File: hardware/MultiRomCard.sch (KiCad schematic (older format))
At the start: 18 parts, among them P1 VC4000_Cartridge_Bus, P2 MicroSD_Breakout, P3 Test Header, U1 Arduino_Nano, U2 74HC595, U3 74HC595, U4 74HC595, U5 6264, U6 74HC245, U7 74HC245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

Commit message: [SCH/PCB] Rotate MicroSD breakout header.
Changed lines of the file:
@@
 Sheet 1 1
 Title "Interton VC4000 MultiRom Cartridge"
-Date "Wednesday, July 22, 2015"
+Date "Tuesday, July 28, 2015"
 Rev "0.1"
 Comp "Mario Keller and Johannes Maibaum"
@@
 	1600 2350 1600 1650
 Wire Wire Line
-	1500 2250 2600 2250
-Wire Wire Line
-	2600 2250 2600 3300
+	2600 1950 2600 3300
 Wire Wire Line
 	2600 3300 2200 3300
 Wire Wire Line
-	1500 1950 2300 1950
-Wire Wire Line
-	2300 1950 2300 3000
-Wire Wire Line
-	2300 3000 2200 3000
-Wire Wire Line
-	1500 2050 2400 2050
-Wire Wire Line
-	2400 2050 2400 3100
-Wire Wire Line
-	2400 3100 2200 3100
+	2200 3000 2300 3000
+Wire Wire Line
+	1500 2050 2300 2050
+Wire Wire Line
+	2300 2050 2300 3000
 Wire Wire Line
 	1500 2150 2500 2150
@@
 	1    1600 1650
 	1    0    0    -1
-$EndComp
-$Comp
-L MicroSD_Breakout P2
-U 1 1 55880347
-P 1300 2200
-F 0 "P2" H 1400 2550 60  0000 C CNN
-F 1 "MicroSD_Breakout" V 1600 2200 60  0000 C CNN
-F 2 "Pin_Headers:Pin_Header_Straight_1x06" H 1300 2200 60  0001 C CNN
-F 3 "" H 1300 2200 60  0000 C CNN
-	1    1300 2200
-	-1   0    0    -1
 $EndComp
 NoConn ~ 900  3800
@@
 Wire Wire Line
 	9750 3750 9750 3900
+$Comp
+L MicroSD_Breakout P2
+U 1 1 55B39402
+P 1300 2200
+F 0 "P2" H 1400 2550 60  0000 C CNN
+F 1 "MicroSD_Breakout" V 1600 2200 60  0000 C CNN
+F 2 "Pin_Headers:Pin_Header_Straight_1x06" H 1300 2200 60  0001 C CNN
+F 3 "" H 1300 2200 60  0000 C CNN
+	1    1300 2200
+	-1   0    0    -1
+$EndComp
+Wire Wire Line
+	2600 1950 1500 1950
+Wire Wire Line
+	1500 2250 2400 2250
+Wire Wire Line
+	2400 2250 2400 3100
+Wire Wire Line
+	2400 3100 2200 3100
 $EndSCHEMATC

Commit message: [HW/FW] Incorporate latest changes into hardware and firmware.
- From now on, we should call the hardware rev. 0.2.
- All games should now work (ROM and ROM+RAM)
- Up to 6K (5.5K) ROM is currently allowed (7.5K should be
  possible, too, with one line change in the FW.)
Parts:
- removed P3: Test Header, Pin_Headers:Pin_Header_Straight_1x30, symbol CONN_01X30
- added C8, C9: .1uF, Capacitors_ThroughHole:C_Disc_D6_P5, symbol C
- added R1: 10k, Resistors_ThroughHole:Resistor_Horizontal_RM10mm, symbol R
- added U10: 74HC32, Housings_DIP:DIP-14_W7.62mm_LongPads, symbol 74LS32
- added U9: 74HC00, Housings_DIP:DIP-14_W7.62mm_LongPads, symbol 74HC00
- U2, U3, U4: footprint Housings_DIP:DIP-16__300_ELL -> Housings_DIP:DIP-16_W7.62mm_LongPads
- U5: footprint Housings_DIP:DIP-28__600_ELL -> Housings_DIP:DIP-28_W15.24mm_LongPads
- U6, U7, U8: footprint Housings_DIP:DIP-20__300_ELL -> Housings_DIP:DIP-20_W7.62mm_LongPads
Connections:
- net labels added: CE1, CEDBUS, RW, WCONTROL, WRP
- net labels removed: CE1SRAM, CE2, CE2SRAM, P26, P27, P28, PVISEL
- wire segments 236 -> 204
- no-connect marks 20 -> 24
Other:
- moved on the sheet: C1, C2, C3, C4, C5, C6, C7, U6, U7, U8

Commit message: [HW] A little cleanup on the schematic, new PDF printouts.
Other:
- moved on the sheet: R1, U10A, U9A
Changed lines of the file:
@@
 Sheet 1 1
 Title "Interton VC4000 MultiRom Cartridge"
-Date "Monday, August 3, 2015"
+Date "Tuesday, August 4, 2015"
 Rev "0.2"
 Comp "Mario Keller and Johannes Maibaum"
@@
 	1    0    0    -1
 $EndComp
-Text GLabel 6700 3700 2    48   Input ~ 0
+Text GLabel 6700 3500 2    48   Input ~ 0
 WESRAM
 Text GLabel 2200 3300 2    48   Output ~ 0
@@
 Text GLabel 9500 3350 1    48   Input ~ 0
 OEVCBUS
-Text GLabel 5500 4700 0    48   Input ~ 0
+Text GLabel 5500 5150 0    48   Input ~ 0
 OEVCBUS
 Text GLabel 9550 1400 2    48   Input ~ 0
@@
 L R R1
 U 1 1 55BBBA81
-P 7150 3750
-F 0 "R1" V 7230 3750 50  0000 C CNN
-F 1 "10k" V 7150 3750 50  0000 C CNN
-F 2 "Resistors_ThroughHole:Resistor_Horizontal_RM10mm" V 7080 3750 30  0001 C CNN
-F 3 "" H 7150 3750 30  0000 C CNN
-	1    7150 3750
+P 7150 3900
+F 0 "R1" V 7230 3900 50  0000 C CNN
+F 1 "10k" V 7150 3900 50  0000 C CNN
+F 2 "Resistors_ThroughHole:Resistor_Horizontal_RM10mm" V 7080 3900 30  0001 C CNN
+F 3 "" H 7150 3900 30  0000 C CNN
+	1    7150 3900
 	1    0    0    -1
 $EndComp
@@
 L GND #PWR012
 U 1 1 55BBBD64
-P 7150 3900
-F 0 "#PWR012" H 7150 3900 30  0001 C CNN
-F 1 "GND" H 7150 3830 30  0001 C CNN
-F 2 "" H 7150 3900 60  0000 C CNN
-F 3 "" H 7150 3900 60  0000 C CNN
-	1    7150 3900
+P 7150 4050
+F 0 "#PWR012" H 7150 4050 30  0001 C CNN
+F 1 "GND" H 7150 3980 30  0001 C CNN
+F 2 "" H 7150 4050 60  0000 C CNN
+F 3 "" H 7150 4050 60  0000 C CNN
+	1    7150 4050
 	1    0    0    -1
 $EndComp
@@
 L 74HC00 U9
 U 1 1 55BBD9BC
-P 6100 4100
-F 0 "U9" H 6100 4150 60  0000 C CNN
-F 1 "74HC00" H 6100 4050 60  0000 C CNN
-F 2 "Housings_DIP:DIP-14_W7.62mm_LongPads" H 6100 4100 60  0001 C CNN
-F 3 "" H 6100 4100 60  0000 C CNN
-	1    6100 4100
+P 6100 4550
+F 0 "U9" H 6100 4600 60  0000 C CNN
+F 1 "74HC00" H 6100 4500 60  0000 C CNN
+F 2 "Housings_DIP:DIP-14_W7.62mm_LongPads" H 6100 4550 60  0001 C CNN
+F 3 "" H 6100 4550 60  0000 C CNN
+	1    6100 4550
 	-1   0    0    -1
 $EndComp
@@
 L 74LS32 U10
 U 1 1 55BBDA1A
-P 6100 4600
-F 0 "U10" H 6100 4650 60  0000 C CNN
-F 1 "74HC32" H 6100 4550 60  0000 C CNN
-F 2 "Housings_DIP:DIP-14_W7.62mm_LongPads" H 6100 4600 60  0001 C CNN
-F 3 "" H 6100 4600 60  0000 C CNN
-	1    6100 4600
+P 6100 5050
+F 0 "U10" H 6100 5100 60  0000 C CNN
+F 1 "74HC32" H 6100 5000 60  0000 C CNN
+F 2 "Housings_DIP:DIP-14_W7.62mm_LongPads" H 6100 5050 60  0001 C CNN
+F 3 "" H 6100 5050 60  0000 C CNN
+	1    6100 5050
 	1    0    0    -1
 $EndComp
 Text GLabel 9600 4850 2    48   Input ~ 0
 CEDBUS
-Text GLabel 6700 4600 2    48   Output ~ 0
+Text GLabel 6700 5050 2    48   Output ~ 0
 CEDBUS
 $Comp
@@
 U 2 1 55BC3174
 P 9150 850
-F 0 "U9" H 9150 800 60  0000 C CNN
-F 1 "74HC00" H 9150 900 60  0000 C CNN
+F 0 "U9" H 9150 900 60  0000 C CNN
+F 1 "74HC00" H 9150 800 60  0000 C CNN
 F 2 "Housings_DIP:DIP-14_W7.62mm_LongPads" H 9150 850 60  0001 C CNN
 F 3 "" H 9150 850 60  0000 C CNN
 	2    9150 850
-	-1   0    0    1
-$EndComp
+	-1   0    0    -1
+$EndComp
+Text Label 9750 950  0    60   ~ 0
+WRP
 Text Label 9750 750  0    60   ~ 0
-WRP
-Text Label 9750 950  0    60   ~ 0
 RW
 Entry Wire Line
@@
 U 2 1 55BC41B8
 P 6100 3600
-F 0 "U10" H 6100 3550 60  0000 C CNN
-F 1 "74HC32" H 6100 3650 60  0000 C CNN
+F 0 "U10" H 6100 3650 60  0000 C CNN
+F 1 "74HC32" H 6100 3550 60  0000 C CNN
 F 2 "Housings_DIP:DIP-14_W7.62mm_LongPads" H 6100 3600 60  0001 C CNN
 F 3 "" H 6100 3600 60  0000 C CNN
 	2    6100 3600
-	-1   0    0    1
+	-1   0    0    -1
 $EndComp
 NoConn ~ 10550 2350
@@
 Connection ~ 2700 7150
 Wire Wire Line
-	5400 4500 5500 4500
-Wire Wire Line
-	5400 4100 5400 4500
+	5400 4950 5500 4950
+Wire Wire Line
+	5400 4550 5400 4950
 Wire Wire Line
 	9300 4850 9600 4850
@@
 	4950 3000 3350 3000
 Wire Wire Line
-	5400 4100 5500 4100
+	5400 4550 5500 4550
 Wire Wire Line
 	9300 4350 9750 4350
@@
 	9750 750  9950 750
 Wire Wire Line
-	6700 4000 6700 4200
-Connection ~ 6700 4100
+	6700 4450 6700 4650
+Connection ~ 6700 4550
 Wire Wire Line
 	5400 3350 5400 3600
@@
 	5050 6050 7700 6050
 Wire Wire Line
-	6700 3500 7700 3500
-Wire Wire Line
-	6700 4100 7700 4100
-Wire Wire Line
-	7700 4100 7700 4150
+	6700 4550 7700 4550
+Wire Wire Line
+	7700 4550 7700 4150
 Wire Wire Line
 	7700 4150 7900 4150
 Wire Wire Line
-	7150 3500 7150 3600
-Wire Wire Line
-	7700 3500 7700 3750
+	7150 3700 7150 3750
+Wire Wire Line
+	7700 3700 7700 3750
 Wire Wire Line
 	7700 3750 7900 3750
-Connection ~ 7150 3500
+Connection ~ 7150 3700
 NoConn ~ 7900 4450
 Wire Wire Line
@@
 	9850 1500 9850 4250
 Wire Bus Line
-	7400 1500 7400 4250
-Wire Bus Line
 	5250 1500 5250 3050
 Wire Bus Line
 	5150 1500 5150 3550
 Wire Bus Line
-	5050 6050 5050 4750
+	5050 4750 5050 6050
+Wire Wire Line
+	6700 3700 7700 3700
+Wire Bus Line
+	7400 1500 7400 4250
 $EndSCHEMATC

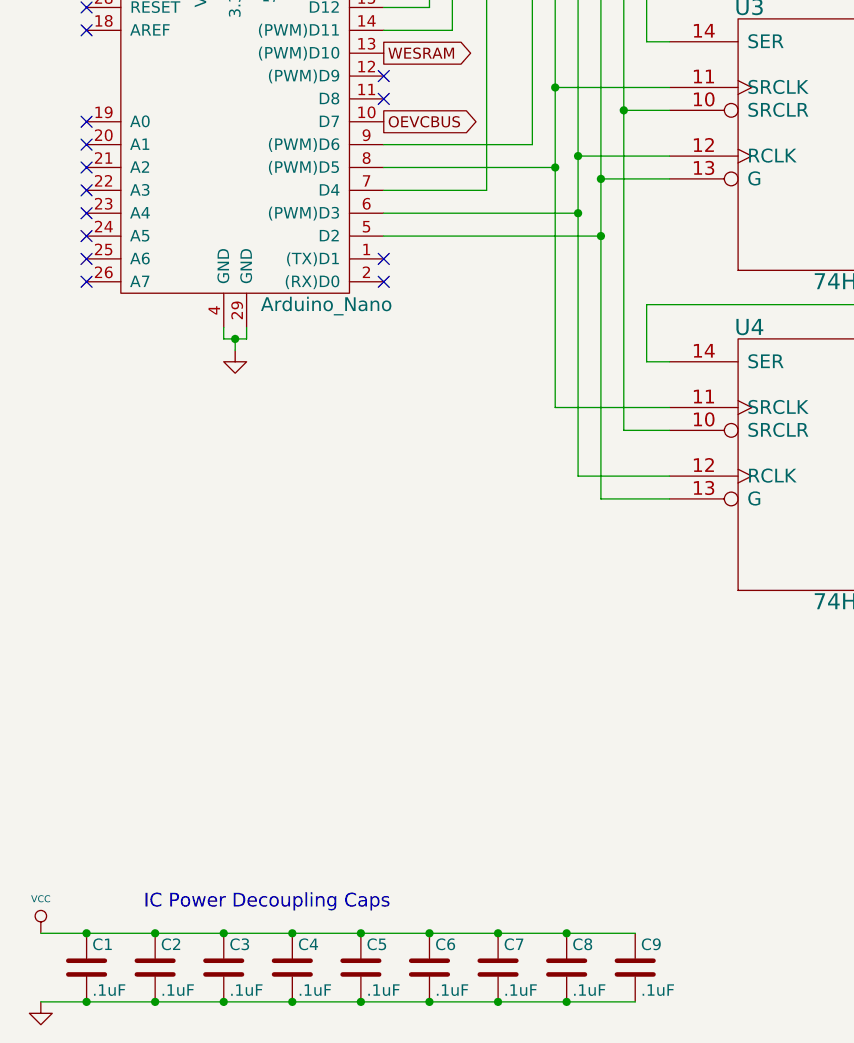
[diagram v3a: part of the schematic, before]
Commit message: added 3 push buttons and a display prot connected to I2C
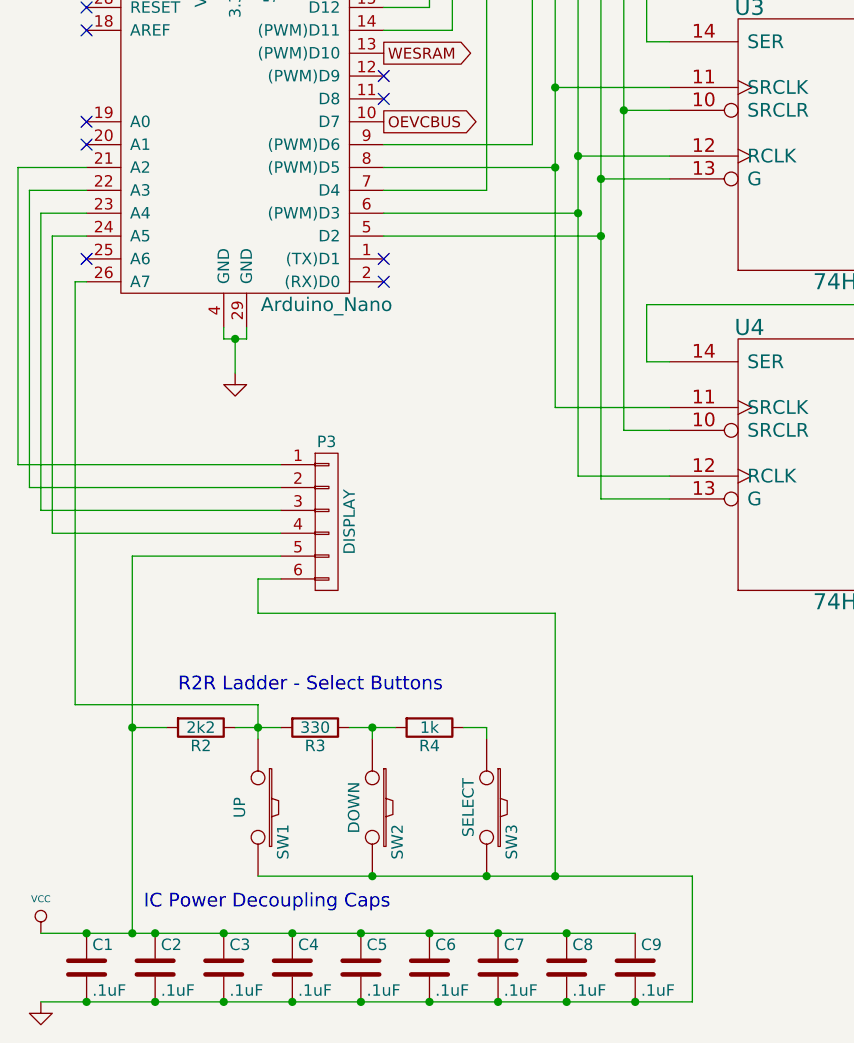
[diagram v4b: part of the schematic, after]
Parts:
- added P3: DISPLAY, Pin_Headers:Pin_Header_Straight_1x06, symbol CONN_01X06
- added R2: 2k2, Resistors_ThroughHole:Resistor_Horizontal_RM10mm, symbol R
- added R3: 330, Resistors_ThroughHole:Resistor_Horizontal_RM10mm, symbol R
- added R4: 1k, Resistors_ThroughHole:Resistor_Horizontal_RM10mm, symbol R
- added SW1: UP, Buttons_Switches_ThroughHole:SW_PUSH_SMALL, symbol SW_PUSH
- added SW2: DOWN, Buttons_Switches_ThroughHole:SW_PUSH_SMALL, symbol SW_PUSH
- added SW3: SELECT, Buttons_Switches_ThroughHole:SW_PUSH_SMALL, symbol SW_PUSH
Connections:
- net GND: now also P3.6 (P6), SW1.2, SW2.2, SW3.2
- net VCC: now also P3.5 (P5), R2.2
- net at U1.21 (A2): now also P3.1 (P1)
- net at U1.22 (A3): now also P3.2 (P2)
- net at U1.23 (A4): now also P3.3 (P3)
- net at U1.24 (A5): now also P3.4 (P4)
- net at U1.26 (A7): now also R2.1, R3.2, SW1.1
- new net: R3.1, R4.2, SW2.1
- new net: R4.1, SW3.1
- no-connect marks 24 -> 19
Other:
- note added: "R2R Ladder - Select Buttons"
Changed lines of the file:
@@
 	1    0    0    -1
 $EndComp
-NoConn ~ 900  4000
-NoConn ~ 900  4100
 NoConn ~ 900  4200
-NoConn ~ 900  4300
 Entry Wire Line
 	10050 4750 10150 4650
@@
 	1    0    0    -1
 $EndComp
-NoConn ~ 900  3800
-NoConn ~ 900  3900
 $Comp
 L GND #PWR010
 U 1 1 54D739DD
-P 1550 4600
-F 0 "#PWR010" H 1550 4600 30  0001 C CNN
-F 1 "GND" H 1550 4530 30  0001 C CNN
-F 2 "" H 1550 4600 60  0000 C CNN
-F 3 "" H 1550 4600 60  0000 C CNN
-	1    1550 4600
+P 1550 4700
+F 0 "#PWR010" H 1550 4700 30  0001 C CNN
+F 1 "GND" H 1550 4630 30  0001 C CNN
+F 2 "" H 1550 4700 60  0000 C CNN
+F 3 "" H 1550 4700 60  0000 C CNN
+	1    1550 4700
 	1    0    0    -1
 $EndComp
@@
 Connection ~ 1550 4550
 Wire Wire Line
-	1550 4550 1550 4600
+	1550 4550 1550 4700
 Wire Wire Line
 	1600 4550 1600 4500
@@
 Connection ~ 1200 7450
 Wire Wire Line
-	700  7450 3300 7450
+	700  7450 3550 7450
 Connection ~ 2400 7150
 Connection ~ 2100 7150
@@
 Wire Bus Line
 	7400 1500 7400 4250
+$Comp
+L R R2
+U 1 1 55D04E06
+P 1400 6250
+F 0 "R2" V 1480 6250 50  0000 C CNN
+F 1 "2k2" V 1400 6250 50  0000 C CNN
+F 2 "Resistors_ThroughHole:Resistor_Horizontal_RM10mm" V 1330 6250 30  0001 C CNN
+F 3 "" H 1400 6250 30  0000 C CNN
+	1    1400 6250
+	0    1    1    0
+$EndComp
+$Comp
+L R R3
+U 1 1 55D04F05
+P 1900 6250
+F 0 "R3" V 1980 6250 50  0000 C CNN
+F 1 "330" V 1900 6250 50  0000 C CNN
+F 2 "Resistors_ThroughHole:Resistor_Horizontal_RM10mm" V 1830 6250 30  0001 C CNN
+F 3 "" H 1900 6250 30  0000 C CNN
+	1    1900 6250
+	0    1    1    0
+$EndComp
+$Comp
+L R R4
+U 1 1 55D04F72
+P 2400 6250
+F 0 "R4" V 2480 6250 50  0000 C CNN
+F 1 "1k" V 2400 6250 50  0000 C CNN
+F 2 "Resistors_ThroughHole:Resistor_Horizontal_RM10mm" V 2330 6250 30  0001 C CNN
+F 3 "" H 2400 6250 30  0000 C CNN
+	1    2400 6250
+	0    1    1    0
+$EndComp
+Wire Wire Line
+	1100 5500 1100 7150
+Wire Wire Line
+	1100 6250 1250 6250
+Connection ~ 1100 7150
+Wire Wire Line
+	1550 6250 1750 6250
+Wire Wire Line
+	2050 6250 2250 6250
+$Comp
+L SW_PUSH SW1
+U 1 1 55D05320
+P 1650 6600
+F 0 "SW1" H 1800 6710 50  0000 C CNN
+F 1 "UP" H 1650 6520 50  0000 C CNN
+F 2 "Buttons_Switches_ThroughHole:SW_PUSH_SMALL" H 1650 6600 60  0001 C CNN
+F 3 "" H 1650 6600 60  0000 C CNN
+	1    1650 6600
+	0    1    1    0
+$EndComp
+$Comp
+L SW_PUSH SW2
+U 1 1 55D05473
+P 2150 6600
+F 0 "SW2" H 2300 6710 50  0000 C CNN
+F 1 "DOWN" H 2150 6520 50  0000 C CNN
+F 2 "Buttons_Switches_ThroughHole:SW_PUSH_SMALL" H 2150 6600 60  0001 C CNN
+F 3 "" H 2150 6600 60  0000 C CNN
+	1    2150 6600
+	0    1    1    0
+$EndComp
+$Comp
+L SW_PUSH SW3
+U 1 1 55D054DB
+P 2650 6600
+F 0 "SW3" H 2800 6710 50  0000 C CNN
+F 1 "SELECT" H 2650 6520 50  0000 C CNN
+F 2 "Buttons_Switches_ThroughHole:SW_PUSH_SMALL" H 2650 6600 60  0001 C CNN
+F 3 "" H 2650 6600 60  0000 C CNN
+	1    2650 6600
+	0    1    1    0
+$EndComp
+Wire Wire Line
+	1650 6900 3550 6900
+Connection ~ 2150 6900
+Wire Wire Line
+	3550 6900 3550 7450
+Connection ~ 3300 7450
+Connection ~ 2650 6900
+Wire Wire Line
+	1650 6150 1650 6300
+Connection ~ 1650 6250
+Wire Wire Line
+	2150 6300 2150 6250
+Connection ~ 2150 6250
+Wire Wire Line
+	2650 6300 2650 6250
+Wire Wire Line
+	2650 6250 2550 6250
+$Comp
+L CONN_01X06 P3
+U 1 1 55D05CFD
+P 1950 5350
+F 0 "P3" H 1950 5700 50  0000 C CNN
+F 1 "DISPLAY" V 2050 5350 50  0000 C CNN
+F 2 "Pin_Headers:Pin_Header_Straight_1x06" H 1950 5350 60  0001 C CNN
+F 3 "" H 1950 5350 60  0000 C CNN
+	1    1950 5350
+	1    0    0    -1
+$EndComp
+Wire Wire Line
+	1750 5600 1650 5600
+Wire Wire Line
+	1650 5600 1650 5750
+Wire Wire Line
+	1650 5750 2950 5750
+Wire Wire Line
+	2950 5750 2950 6900
+Connection ~ 2950 6900
+Wire Wire Line
+	1750 5500 1100 5500
+Connection ~ 1100 6250
+Wire Wire Line
+	900  4300 850  4300
+Wire Wire Line
+	850  4300 850  6150
+Wire Wire Line
+	850  6150 1650 6150
+Wire Wire Line
+	900  4100 750  4100
+Wire Wire Line
+	750  4100 750  5400
+Wire Wire Line
+	750  5400 1750 5400
+Wire Wire Line
+	900  4000 700  4000
+Wire Wire Line
+	700  4000 700  5300
+Wire Wire Line
+	700  5300 1750 5300
+Wire Wire Line
+	900  3900 650  3900
+Wire Wire Line
+	650  3900 650  5200
+Wire Wire Line
+	650  5200 1750 5200
+Wire Wire Line
+	900  3800 600  3800
+Wire Wire Line
+	600  3800 600  5100
+Wire Wire Line
+	600  5100 1750 5100
+Text Notes 1300 6100 0    60   ~ 0
+R2R Ladder - Select Buttons
 $EndSCHEMATC
